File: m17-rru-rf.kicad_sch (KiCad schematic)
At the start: 0 parts

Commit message: pcb update
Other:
- note added: "Low power RF tracks: coplanar waveguide Er=4.4, height=0.2104mm 0.25mm track width 0.052mm conductor gap High power RF tracks: coplanar waveguide Er=4.5, height=1.4858mm 2mm track width 0.52mm conductor gap"
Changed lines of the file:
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@@
     (stroke (width 0) (type default))
+  )
+  (text "Low power RF tracks:\ncoplanar waveguide\nEr=4.4, height=0.2104mm\n0.25mm track width\n0.052mm conductor gap\n\nHigh power RF tracks:\ncoplanar waveguide\nEr=4.5, height=1.4858mm\n2mm track width\n0.52mm conductor gap"
+    (at 265.43 279.4 0)
+    (effects (font (size 1.27 1.27)) (justify left bottom))
   )
   (label "SPI_MOSI" (at 129.54 77.47 0) (fields_autoplaced)

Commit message: pcb update
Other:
- added sheet Mechanical (mech.kicad_sch)
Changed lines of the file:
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@@
   (title_block
     (title "M17 Remote Radio Unit - RF board")
-    (date "27-10-2023")
+    (date "28-10-2023")
     (rev "A")
     (company "M17 Project")
@@
   )
   (text "Low power RF tracks:\ncoplanar waveguide\nEr=4.4, height=0.2104mm\n0.25mm track width\n0.052mm conductor gap\n\nHigh power RF tracks:\ncoplanar waveguide\nEr=4.5, height=1.4858mm\n2mm track width\n0.52mm conductor gap"
-    (at 265.43 279.4 0)
-    (effects (font (size 1.27 1.27)) (justify left bottom))
+    (at 31.75 73.66 0)
+    (effects (font (size 2.54 2.54)) (justify left bottom))
   )
   (label "SPI_MOSI" (at 129.54 77.47 0) (fields_autoplaced)
@@
       )
     )
+  )
+  (sheet (at 266.7 254) (size 25.4 25.4) (fields_autoplaced)
+    (stroke (width 0.1524) (type solid))
+    (fill (color 0 0 0 0.0000))
+    (property "Sheetname" "Mechanical" (at 266.7 253.2884 0)
+      (effects (font (size 1.27 1.27)) (justify left bottom))
+    )
+    (property "Sheetfile" "mech.kicad_sch" (at 266.7 279.9846 0)
+      (effects (font (size 1.27 1.27)) (justify left top))
+    )
+    (instances
+      (project "m17-rru-rf"
+        (path "/4c42207c-9e6b-42da-ad38-da126b892014" (page "12"))
+      )
+    )

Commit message: date update
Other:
- title: M17 Remote Radio Unit - RF board -> Remote Radio Unit - RF board
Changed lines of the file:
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@@
   (paper "A3")
   (title_block
-    (title "M17 Remote Radio Unit - RF board")
-    (date "28-10-2023")
+    (title "Remote Radio Unit - RF board")
+    (date "30-10-2023")
     (rev "A")
     (company "M17 Project")

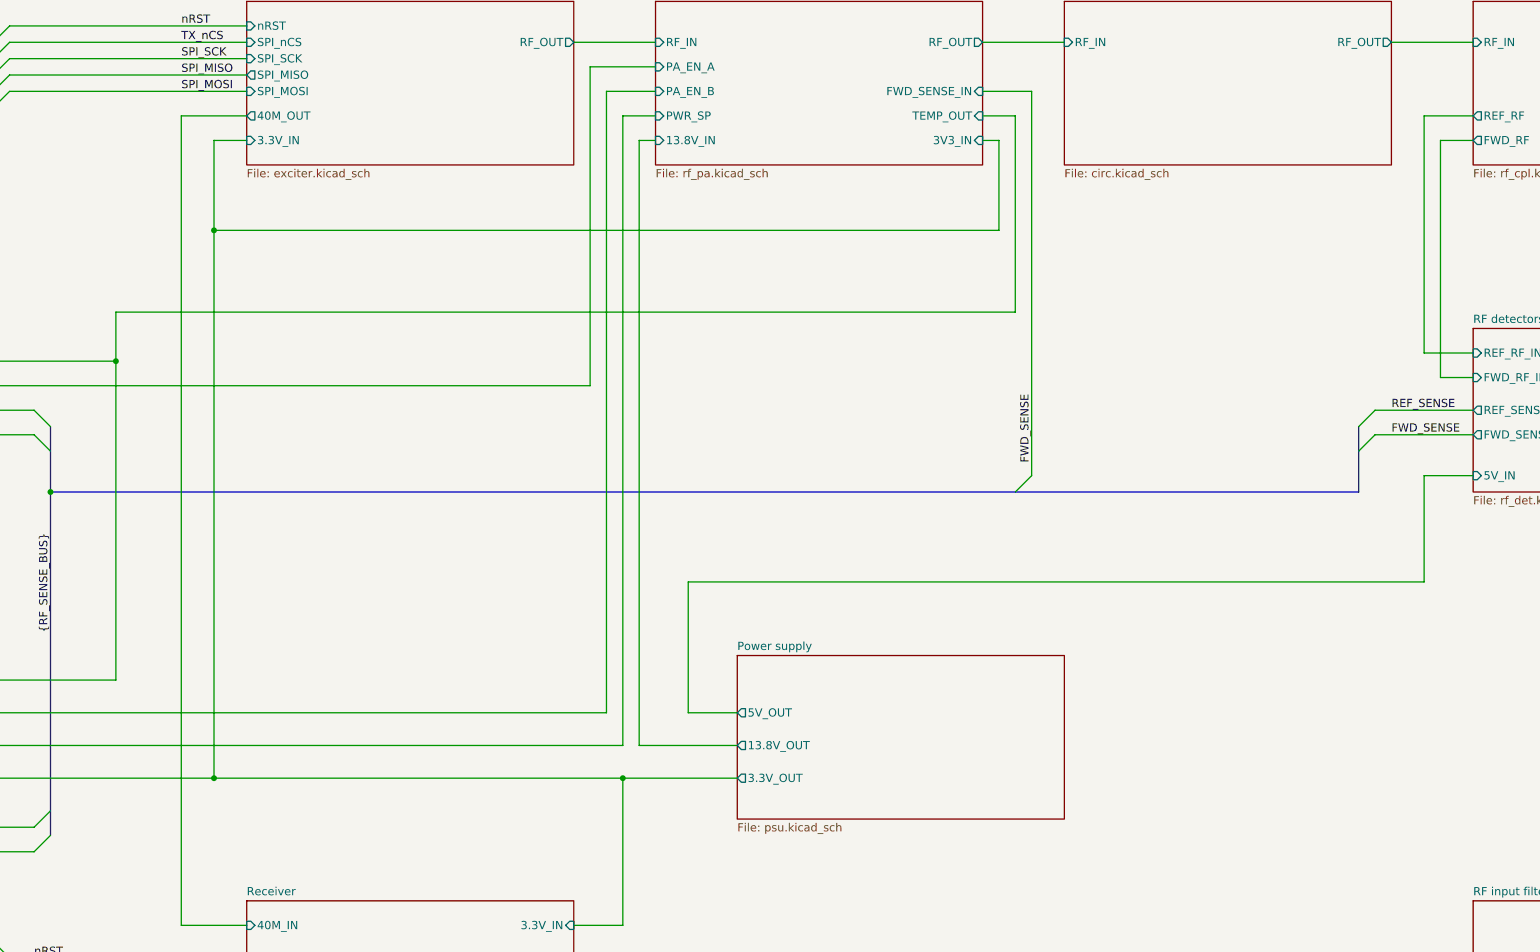
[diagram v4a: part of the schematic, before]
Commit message: some via fencing
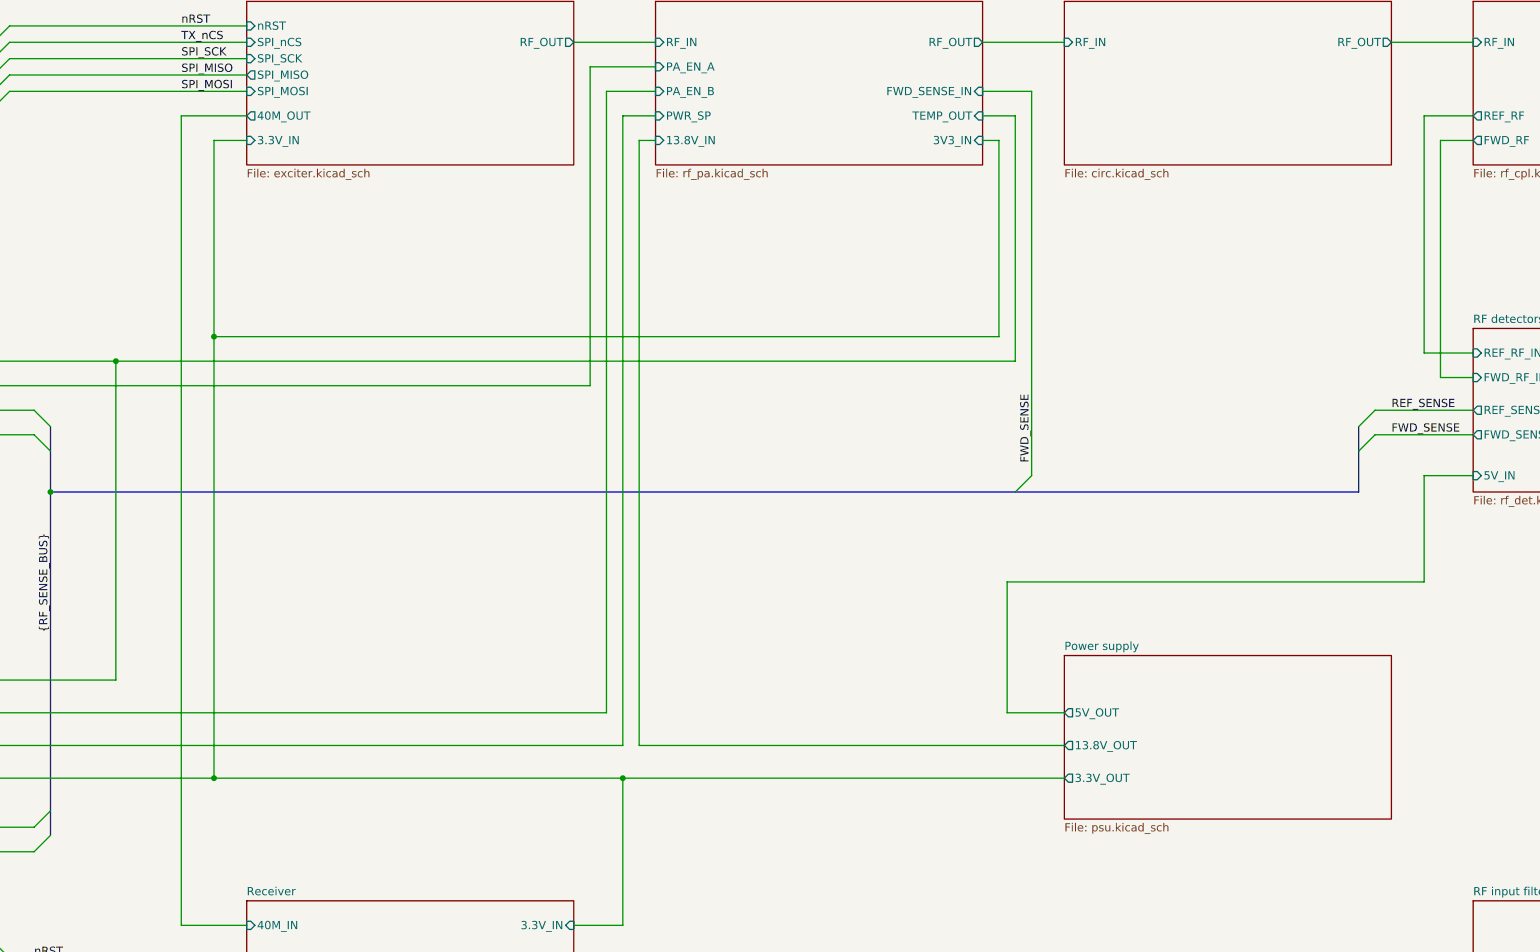
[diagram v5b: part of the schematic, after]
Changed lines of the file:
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@@
   (title_block
     (title "Remote Radio Unit - RF board")
-    (date "30-10-2023")
+    (date "31-10-2023")
     (rev "A")
     (company "M17 Project")
@@
   (junction (at 109.22 139.7) (diameter 0) (color 0 0 0 0)
   )
-  (junction (at 134.62 99.06) (diameter 0) (color 0 0 0 0)
-  )
   (junction (at 92.71 184.15) (diameter 0) (color 0 0 0 0)
   )
@@
   (junction (at 198.12 184.15) (diameter 0) (color 0 0 0 0)
   )
+  (junction (at 134.62 115.57) (diameter 0) (color 0 0 0 0)
+  )
   (bus_entry (at 109.22 193.04) (size -2.54 2.54)
     (stroke (width 0) (type default))
@@
     (stroke (width 0) (type default))
   )
-  (wire (pts (xy 259.08 81.28) (xy 259.08 111.76))
+  (wire (pts (xy 259.08 81.28) (xy 259.08 119.38))
     (stroke (width 0) (type default))
   )
@@
     (stroke (width 0) (type default))
   )
-  (wire (pts (xy 256.54 99.06) (xy 134.62 99.06))
+  (wire (pts (xy 256.54 115.57) (xy 134.62 115.57))
     (stroke (width 0) (type default))
   )
@@
     (stroke (width 0) (type default))
   )
-  (wire (pts (xy 134.62 99.06) (xy 134.62 184.15))
-    (stroke (width 0) (type default))
-  )
-  (wire (pts (xy 208.28 153.67) (xy 322.58 153.67))
-    (stroke (width 0) (type default))
-  )
-  (wire (pts (xy 208.28 173.99) (xy 208.28 153.67))
+  (wire (pts (xy 257.81 153.67) (xy 322.58 153.67))
+    (stroke (width 0) (type default))
+  )
+  (wire (pts (xy 257.81 173.99) (xy 257.81 153.67))
     (stroke (width 0) (type default))
   )
@@
     (stroke (width 0) (type default))
   )
-  (wire (pts (xy 134.62 85.09) (xy 134.62 99.06))
+  (wire (pts (xy 134.62 85.09) (xy 134.62 115.57))
     (stroke (width 0) (type default))
   )
@@
     (stroke (width 0) (type default))
   )
-  (wire (pts (xy 256.54 85.09) (xy 256.54 99.06))
+  (wire (pts (xy 256.54 85.09) (xy 256.54 115.57))
     (stroke (width 0) (type default))
   )
@@
     (stroke (width 0) (type default))
   )
-  (wire (pts (xy 200.66 179.07) (xy 215.9 179.07))
+  (wire (pts (xy 200.66 179.07) (xy 266.7 179.07))
     (stroke (width 0) (type default))
   )
@@
     (stroke (width 0) (type default))
   )
-  (wire (pts (xy 119.38 111.76) (xy 119.38 119.38))
-    (stroke (width 0) (type default))
-  )
   (wire (pts (xy 325.12 121.92) (xy 330.2 121.92))
     (stroke (width 0) (type default))
@@
     (stroke (width 0) (type default))
   )
-  (wire (pts (xy 198.12 184.15) (xy 215.9 184.15))
+  (wire (pts (xy 198.12 184.15) (xy 266.7 184.15))
     (stroke (width 0) (type default))
   )
@@
     (stroke (width 0) (type default))
   )
-  (wire (pts (xy 215.9 173.99) (xy 208.28 173.99))
+  (wire (pts (xy 266.7 173.99) (xy 257.81 173.99))
     (stroke (width 0) (type default))
   )
@@
     (stroke (width 0) (type default))
   )
+  (wire (pts (xy 134.62 115.57) (xy 134.62 184.15))
+    (stroke (width 0) (type default))
+  )
   (wire (pts (xy 86.36 146.05) (xy 86.36 163.83))
     (stroke (width 0) (type default))
@@
     (stroke (width 0) (type default))
   )
-  (wire (pts (xy 259.08 111.76) (xy 119.38 111.76))
+  (wire (pts (xy 259.08 119.38) (xy 119.38 119.38))
     (stroke (width 0) (type default))
   )
@@
     )
   )
-  (sheet (at 215.9 165.1) (size 50.8 25.4) (fields_autoplaced)
+  (sheet (at 266.7 165.1) (size 50.8 25.4) (fields_autoplaced)
     (stroke (width 0.1524) (type solid))
     (fill (color 0 0 0 0.0000))
-    (property "Sheetname" "Power supply" (at 215.9 164.3884 0)
+    (property "Sheetname" "Power supply" (at 266.7 164.3884 0)
       (effects (font (size 1.27 1.27)) (justify left bottom))
     )
-    (property "Sheetfile" "psu.kicad_sch" (at 215.9 191.0846 0)
+    (property "Sheetfile" "psu.kicad_sch" (at 266.7 191.0846 0)
       (effects (font (size 1.27 1.27)) (justify left top))
     )
-    (pin "13.8V_OUT" output (at 215.9 179.07 180)
-      (effects (font (size 1.27 1.27)) (justify left))
-    )
-    (pin "3.3V_OUT" output (at 215.9 184.15 180)
-      (effects (font (size 1.27 1.27)) (justify left))
-    )
-    (pin "5V_OUT" output (at 215.9 173.99 180)
-      (effects (font (size 1.27 1.27)) (justify left))
-    )
+    (pin "13.8V_OUT" output (at 266.7 179.07 180)
+      (effects (font (size 1.27 1.27)) (justify left))
+    )
+    (pin "3.3V_OUT" output (at 266.7 184.15 180)
+      (effects (font (size 1.27 1.27)) (justify left))
+    )
+    (pin "5V_OUT" output (at 266.7 173.99 180)
+      (effects (font (size 1.27 1.27)) (justify left))
+    )

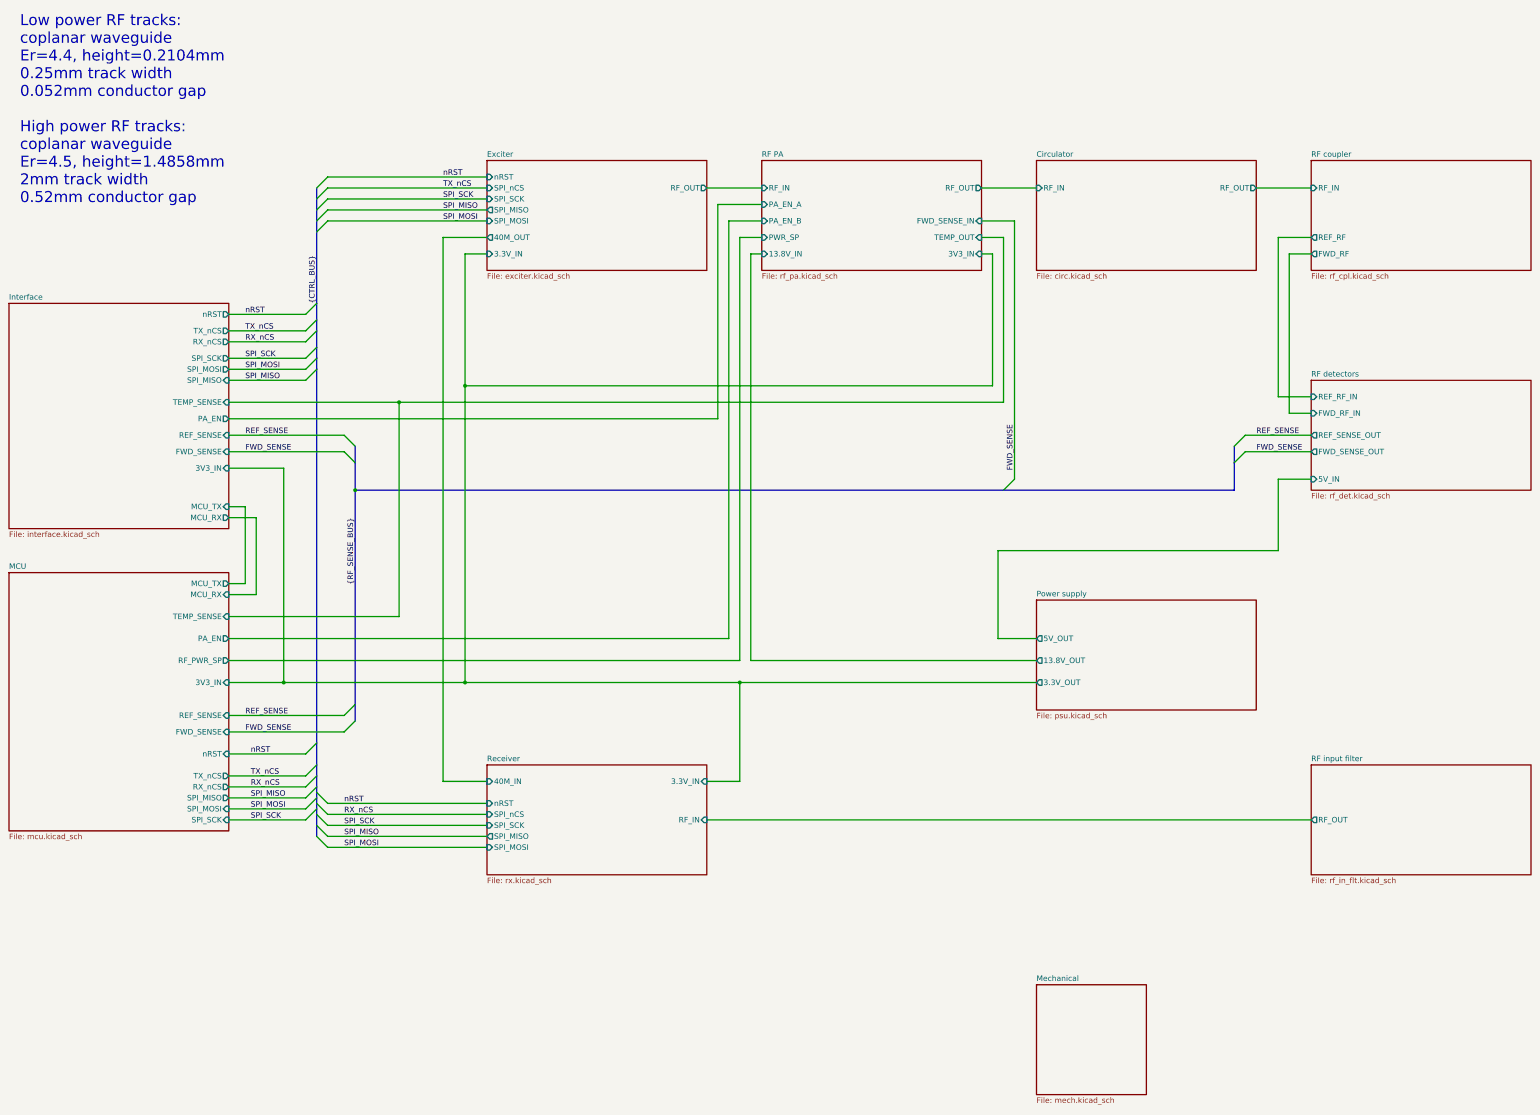
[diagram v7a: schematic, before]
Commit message: WIP rev B
- replaced R44-R46 with 22k
- exposed BOOT0 at the DA15 connector
- added a testpoint at DAC OUT2
- added a buffer to the 40MHz reference oscillator
- removed C2
- bypassed R5 with a 100nF capacitor
- changed D5's voltage to 5.1V
- routed TX_SAMP_CLK
- changed temperature sensor's supply voltage to 5V
- added a series of 100p, 1n and 10n capacitors at PA_VGG
- reduced N-connector cutouts to 2.5mm
- improved RF output track a little
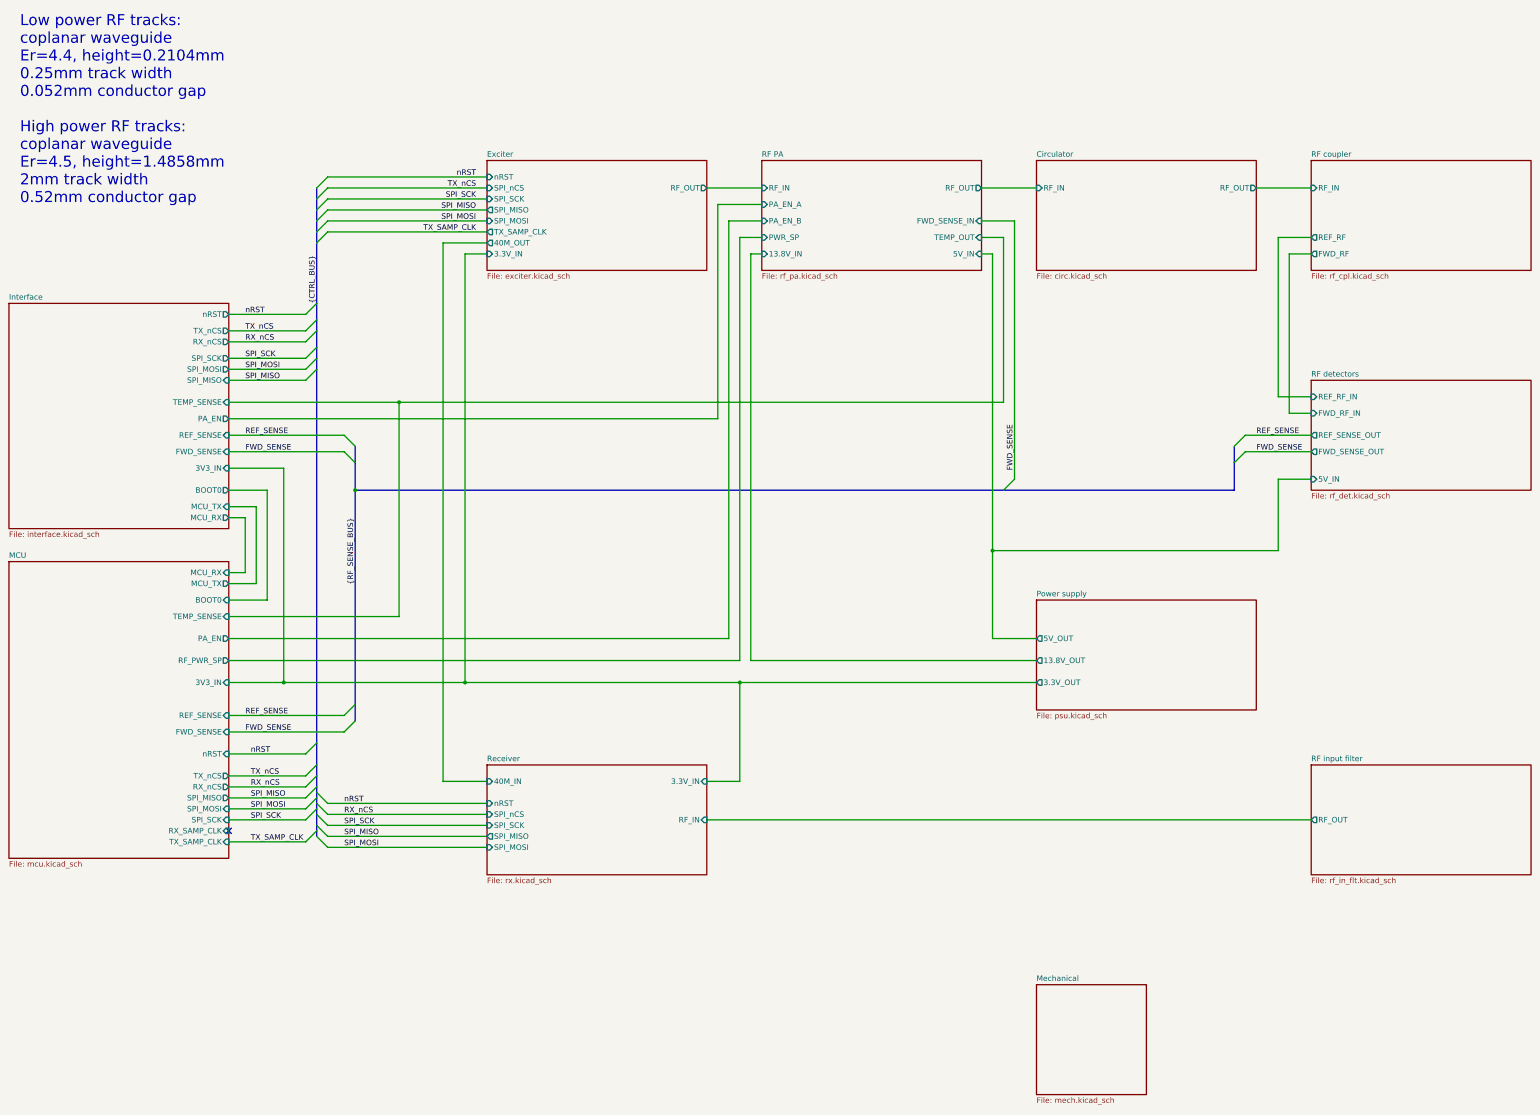
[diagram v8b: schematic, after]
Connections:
- no-connect marks 0 -> 1
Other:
- sheet Exciter ports: added TX_SAMP_CLK; removed none
- sheet Interface ports: added BOOT0; removed none
- sheet MCU ports: added BOOT0, RX_SAMP_CLK, TX_SAMP_CLK; removed none
- sheet RF PA ports: added 5V_IN; removed 3V3_IN
